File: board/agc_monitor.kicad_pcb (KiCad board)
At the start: 4 copper layers, 149.9 x 74.3 mm, 60 parts, among them J1 Conn_01x03, J2 Conn_01x03, J3 Conn_01x10, J4 Styx_P4, J5 Styx_P5, P1 test_connector, Q1 MMBT3904, Q2 MMBT3904, Q3 MMBT3904, Q4 MMBT3904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

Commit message: Board: Added initial rouuting of 3.3V I/O power
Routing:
- net +3V3_IO: track 25.2 -> 188.0 mm, vias 0 -> 8
- added copper zone on In2.Cu, net +3V3_IO
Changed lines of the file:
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@@
     (thickness 1.6)
     (drawings 9)
-    (tracks 1874)
+    (tracks 1921)
     (zones 0)
     (modules 60)
@@
   )
   (setup
-    (last_trace_width 0.1524)
+    (last_trace_width 0.254)
     (user_trace_width 0.1524)
     (user_trace_width 0.2032)
@@
   (segment (start 190.1825 117.7925) (end 180.4035 117.7925) (width 0.1524) (layer In2.Cu) (net 175))
   (segment (start 180.4035 117.7925) (end 174.5615 123.6345) (width 0.1524) (layer In2.Cu) (net 175))
+  (segment (start 145.415 92.45) (end 144.145 92.45) (width 0.254) (layer B.Cu) (net 175))
+  (segment (start 144.145 92.45) (end 142.875 92.45) (width 0.254) (layer B.Cu) (net 175))
+  (segment (start 142.875 92.45) (end 141.605 92.45) (width 0.254) (layer B.Cu) (net 175))
+  (segment (start 141.605 92.45) (end 136.525 92.45) (width 0.254) (layer B.Cu) (net 175))
+  (segment (start 136.525 92.45) (end 137.795 92.45) (width 0.254) (layer F.Cu) (net 175))
+  (segment (start 137.795 92.45) (end 139.065 92.45) (width 0.254) (layer F.Cu) (net 175))
+  (segment (start 139.065 92.45) (end 145.415 92.45) (width 0.254) (layer F.Cu) (net 175))
+  (segment (start 135.642 92.45) (end 136.525 92.45) (width 0.254) (layer B.Cu) (net 175))
+  (segment (start 135.636 92.456) (end 135.642 92.45) (width 0.254) (layer B.Cu) (net 175))
+  (segment (start 136.519 92.456) (end 136.525 92.45) (width 0.254) (layer F.Cu) (net 175))
+  (via (at 135.636 92.456) (size 0.6096) (drill 0.3048) (layers F.Cu B.Cu) (net 175))
+  (segment (start 135.636 92.456) (end 136.519 92.456) (width 0.254) (layer F.Cu) (net 175))
+  (segment (start 132.461 92.45) (end 123.571 92.45) (width 0.254) (layer F.Cu) (net 175))
+  (segment (start 132.461 92.45) (end 123.571 92.45) (width 0.254) (layer B.Cu) (net 175))
+  (via (at 132.461 91.059) (size 0.6096) (drill 0.3048) (layers F.Cu B.Cu) (net 175))
+  (segment (start 132.461 92.45) (end 132.461 91.059) (width 0.254) (layer B.Cu) (net 175))
+  (segment (start 132.461 91.059) (end 132.461 92.45) (width 0.254) (layer F.Cu) (net 175))
+  (segment (start 119.507 92.45) (end 110.617 92.45) (width 0.254) (layer F.Cu) (net 175))
+  (segment (start 110.617 92.45) (end 119.507 92.45) (width 0.254) (layer B.Cu) (net 175))
+  (via (at 119.507 91.059) (size 0.6096) (drill 0.3048) (layers F.Cu B.Cu) (net 175))
+  (segment (start 119.507 92.45) (end 119.507 91.059) (width 0.254) (layer F.Cu) (net 175))
+  (segment (start 119.507 91.059) (end 119.507 92.45) (width 0.254) (layer B.Cu) (net 175))
+  (segment (start 106.553 92.45) (end 97.663 92.45) (width 0.254) (layer B.Cu) (net 175))
+  (segment (start 97.663 92.45) (end 106.553 92.45) (width 0.254) (layer F.Cu) (net 175))
+  (via (at 106.553 91.059) (size 0.6096) (drill 0.3048) (layers F.Cu B.Cu) (net 175))
+  (segment (start 106.553 92.45) (end 106.553 91.059) (width 0.254) (layer F.Cu) (net 175))
+  (segment (start 106.553 91.059) (end 106.553 92.45) (width 0.254) (layer B.Cu) (net 175))
+  (segment (start 145.415 110.75) (end 136.525 110.75) (width 0.254) (layer F.Cu) (net 175))
+  (segment (start 136.525 110.75) (end 145.415 110.75) (width 0.254) (layer B.Cu) (net 175))
+  (segment (start 132.461 110.75) (end 123.571 110.75) (width 0.254) (layer F.Cu) (net 175))
+  (segment (start 123.571 110.75) (end 132.461 110.75) (width 0.254) (layer B.Cu) (net 175))
+  (segment (start 119.507 110.75) (end 110.617 110.75) (width 0.254) (layer F.Cu) (net 175))
+  (segment (start 110.617 110.75) (end 119.507 110.75) (width 0.254) (layer B.Cu) (net 175))
+  (segment (start 106.553 110.75) (end 97.663 110.75) (width 0.254) (layer B.Cu) (net 175))
+  (segment (start 97.663 110.75) (end 106.553 110.75) (width 0.254) (layer F.Cu) (net 175))
+  (via (at 140.335 112.141) (size 0.6096) (drill 0.3048) (layers F.Cu B.Cu) (net 175))
+  (segment (start 140.335 110.75) (end 140.335 112.141) (width 0.254) (layer F.Cu) (net 175))
+  (segment (start 140.335 112.141) (end 140.335 110.75) (width 0.254) (layer B.Cu) (net 175))
+  (via (at 132.461 112.014) (size 0.6096) (drill 0.3048) (layers F.Cu B.Cu) (net 175))
+  (segment (start 132.461 110.75) (end 132.461 112.014) (width 0.254) (layer B.Cu) (net 175))
+  (segment (start 132.461 112.014) (end 132.461 110.75) (width 0.254) (layer F.Cu) (net 175))
+  (via (at 119.507 112.0775) (size 0.6096) (drill 0.3048) (layers F.Cu B.Cu) (net 175))
+  (segment (start 119.507 110.75) (end 119.507 112.0775) (width 0.254) (layer F.Cu) (net 175))
+  (segment (start 119.507 112.0775) (end 119.507 110.75) (width 0.254) (layer B.Cu) (net 175))
+  (via (at 106.553 111.9505) (size 0.6096) (drill 0.3048) (layers F.Cu B.Cu) (net 175))
+  (segment (start 106.553 110.75) (end 106.553 111.9505) (width 0.254) (layer B.Cu) (net 175))
+  (segment (start 106.553 111.9505) (end 106.553 110.75) (width 0.254) (layer F.Cu) (net 175))
   (segment (start 144.841 72.644) (end 150.622 72.644) (width 0.1524) (layer F.Cu) (net 176))
   (segment (start 143.51 73.975) (end 144.841 72.644) (width 0.1524) (layer F.Cu) (net 176))
@@
       )
     )
+  )
+  (zone (net 175) (net_name +3V3_IO) (layer In2.Cu) (hatch edge 0.508)
+    (connect_pads (clearance 0.254))
+    (min_thickness 0.254)
+    (fill yes (arc_segments 16) (thermal_gap 0.508) (thermal_bridge_width 0.508))
+    (polygon
+      (pts
+        (xy 88.7095 83.566) (xy 150.495 83.566) (xy 150.495 72.39) (xy 172.5295 72.39) (xy 178.8795 66.04)
+        (xy 227.965 66.04) (xy 227.965 139.065) (xy 178.435 139.065) (xy 172.466 130.81) (xy 154.4955 130.81)
+        (xy 154.4955 119.634) (xy 88.7095 119.634)
+      )
+    )

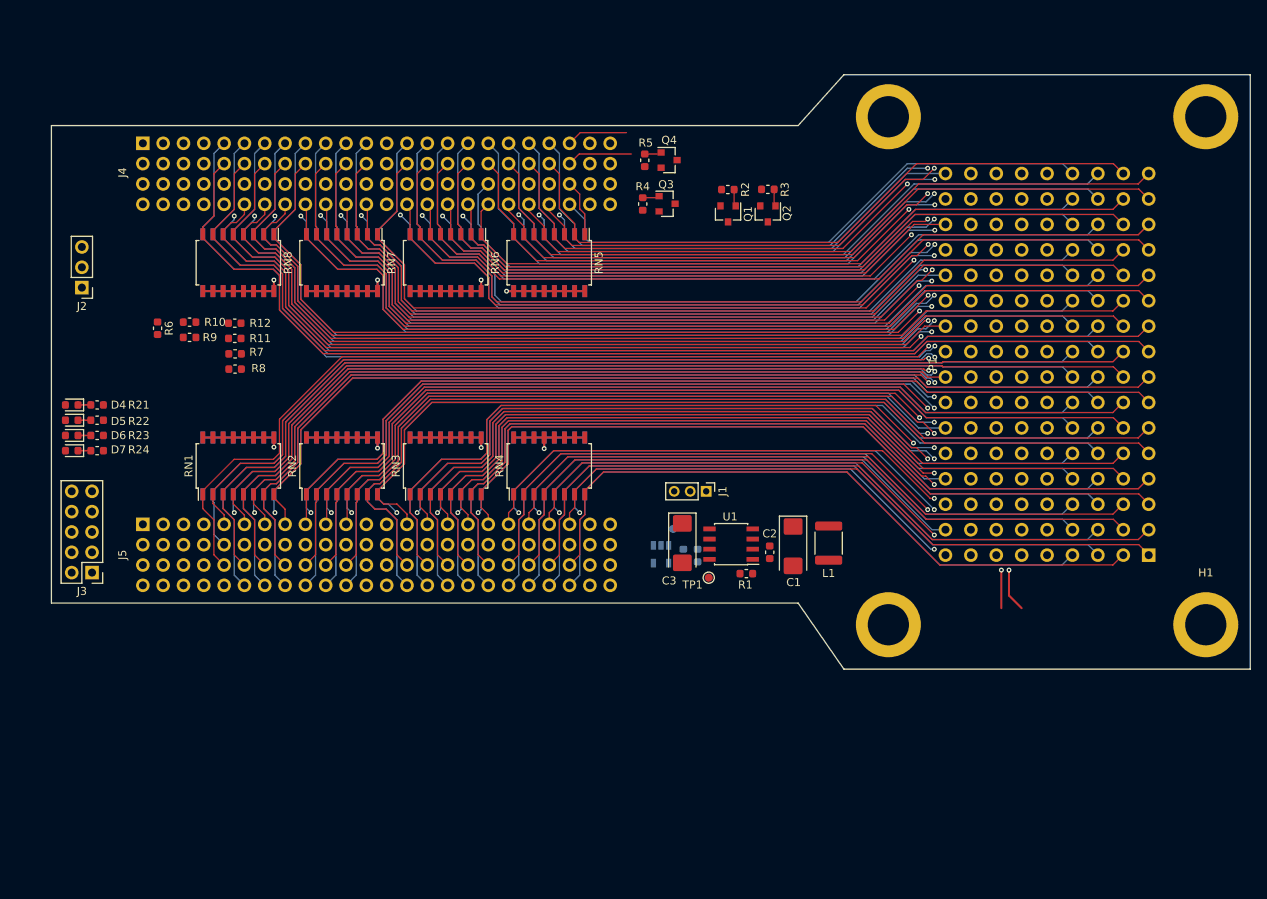
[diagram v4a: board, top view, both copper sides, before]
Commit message: Board: Thinner traces for SI, more layout work, and some 3D models of parts
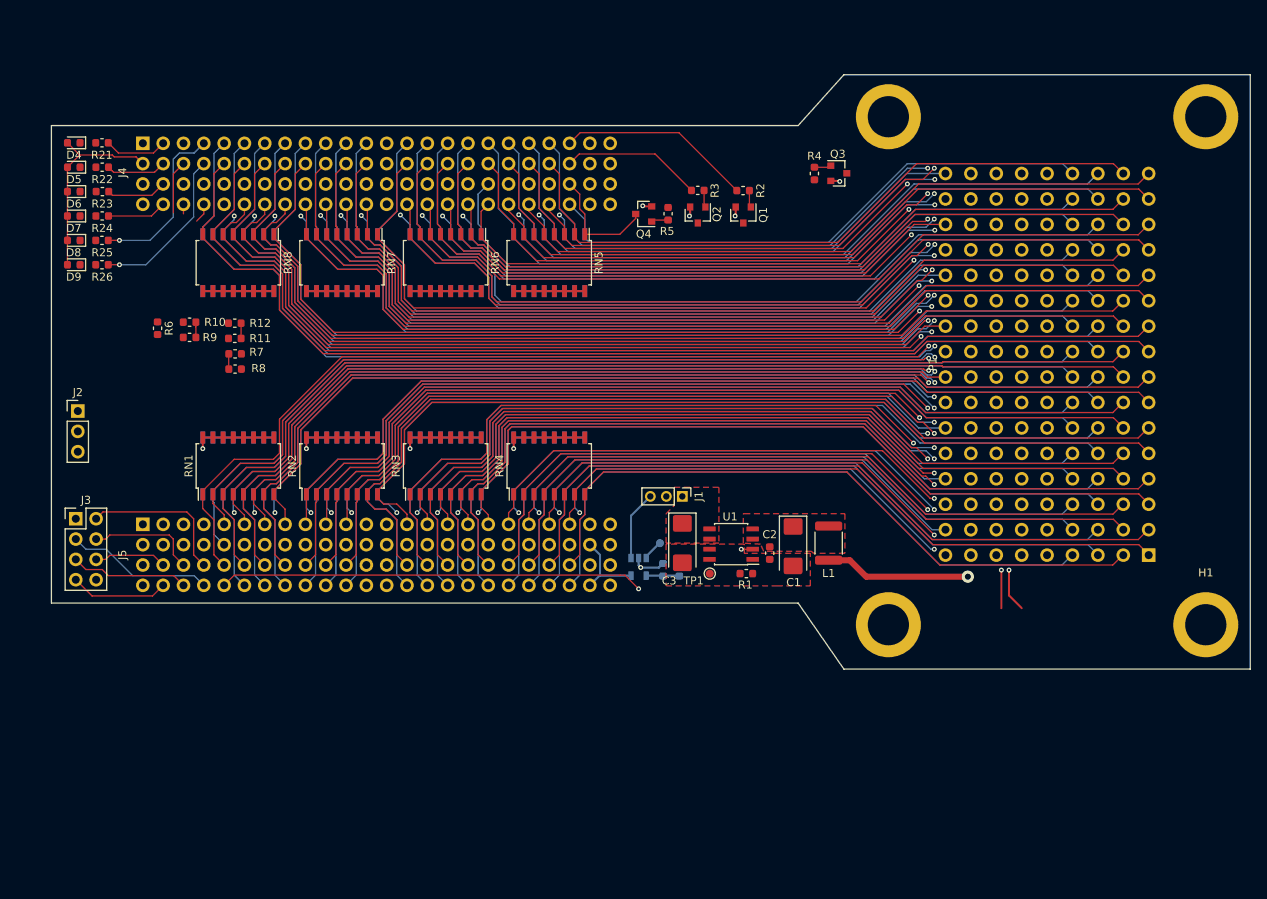
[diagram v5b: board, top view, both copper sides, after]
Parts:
- added D8: LED, LED_SMD:LED_0603_1608Metric, F.Cu at (81.5, 86.1)
- added D9: LED, LED_SMD:LED_0603_1608Metric, F.Cu at (81.5, 89.2)
- added R25: 330, Resistor_SMD:R_0603_1608Metric, F.Cu at (85.1, 86.1)
- added R26: 330, Resistor_SMD:R_0603_1608Metric, F.Cu at (85.1, 89.2)
- J3: value Conn_01x10 -> Conn_01x08; footprint Connector_PinHeader_2.54mm:PinHeader_2x05_P2.54mm_Vertical -> Connector_PinHeader_2.54mm:PinHeader_2x04_P2.54mm_Vertical
- moved R21 32.8 mm to (85.1, 73.9)
- moved D4 32.8 mm to (81.5, 73.9)
- moved R22 31.6 mm to (85.1, 77.0)
- moved D5 31.6 mm to (81.5, 77.0)
- moved R23 30.5 mm to (85.1, 80.0)
- moved D6 30.5 mm to (81.5, 80.0)
- moved R24 29.3 mm to (85.1, 83.1)
- moved D7 29.3 mm to (81.5, 83.1)
- moved Q3 21.8 mm to (177.2, 77.7)
- moved R4 21.8 mm to (174.1, 77.7)
- moved J2 15.4 mm to (82.0, 107.4), turned to 0 degrees
- moved Q2 8.76 mm to (159.5, 82.9)
- moved R3 8.76 mm to (159.5, 79.9)
- moved Q4 7.44 mm to (152.8, 82.8), turned to 180 degrees
- moved R5 7.29 mm to (155.8, 82.8), turned to 90 degrees
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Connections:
- J3 pad 8: /StyxConnectors/DBG7 -> GND
- J4 pad 13: Net-(J4-Pad13) -> /StyxConnectors/LED5
- J4 pad 14: Net-(J4-Pad14) -> /StyxConnectors/LED6
- J4 pad 19: Net-(J4-Pad19) -> GND
- J4 pad 20: Net-(J4-Pad20) -> ADC_3V3_P
- J4 pad 5: Net-(J4-Pad5) -> /StyxConnectors/LED1
- J4 pad 6: Net-(J4-Pad6) -> /StyxConnectors/LED2
- J4 pad 7: Net-(J4-Pad7) -> /StyxConnectors/LED3
- J4 pad 8: Net-(J4-Pad8) -> /StyxConnectors/LED4
- J5 pad 11: Net-(J5-Pad11) -> /StyxConnectors/DBG3
- J5 pad 12: Net-(J5-Pad12) -> /StyxConnectors/DBG4
- J5 pad 15: Net-(J5-Pad15) -> /StyxConnectors/DBG1
- J5 pad 16: Net-(J5-Pad16) -> /StyxConnectors/DBG2
- J5 pad 20: Net-(J5-Pad20) -> EN_3V3_AGC
- J5 pad 7: Net-(J5-Pad7) -> /StyxConnectors/DBG5
- J5 pad 8: Net-(J5-Pad8) -> /StyxConnectors/DBG6
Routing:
- net EN_3V3_AGC: track 0.00 -> 54.5 mm, vias 0 -> 2
- net +3V3_IO: track 188.0 -> 224.9 mm, vias 8 -> 4
- net +3V3_FPGA: track 0.00 -> 34.9 mm
- net +4SW: track 0.00 -> 25.5 mm, vias 0 -> 1
- net /StyxConnectors/LED5: track 0.00 -> 21.2 mm, vias 0 -> 1
- net /StyxConnectors/LED6: track 0.00 -> 20.3 mm, vias 0 -> 1
- net /StyxConnectors/DBG1: track 0.00 -> 19.2 mm
- net /StyxConnectors/DBG2: track 0.00 -> 18.4 mm
- net NHSTRT1: track 7.66 -> 24.5 mm
- net /StyxConnectors/DBG4: track 0.00 -> 14.8 mm
- net /StyxConnectors/DBG3: track 0.00 -> 13.8 mm
- net /StyxConnectors/DBG6: track 0.00 -> 12.3 mm
- net NHSTRT2: track 8.25 -> 17.6 mm
- net /StyxConnectors/DBG5: track 0.00 -> 9.09 mm
- net GND: track 0.00 -> 8.92 mm, vias 0 -> 5
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- added copper zone on F.Cu, net +3V3_AGC
- added copper zone on F.Cu, net GND
- added copper zone on In2.Cu, net GND
- added copper zone on F.Cu, net Net-(C1-Pad1)
- removed copper zone on In2.Cu, net +3V3_FPGA
- removed copper zone on In2.Cu, net +3V3_IO
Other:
- rule trace_min: 0.1524 -> 0.1016

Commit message: Redid the mechanical outline of the board; further development/layout
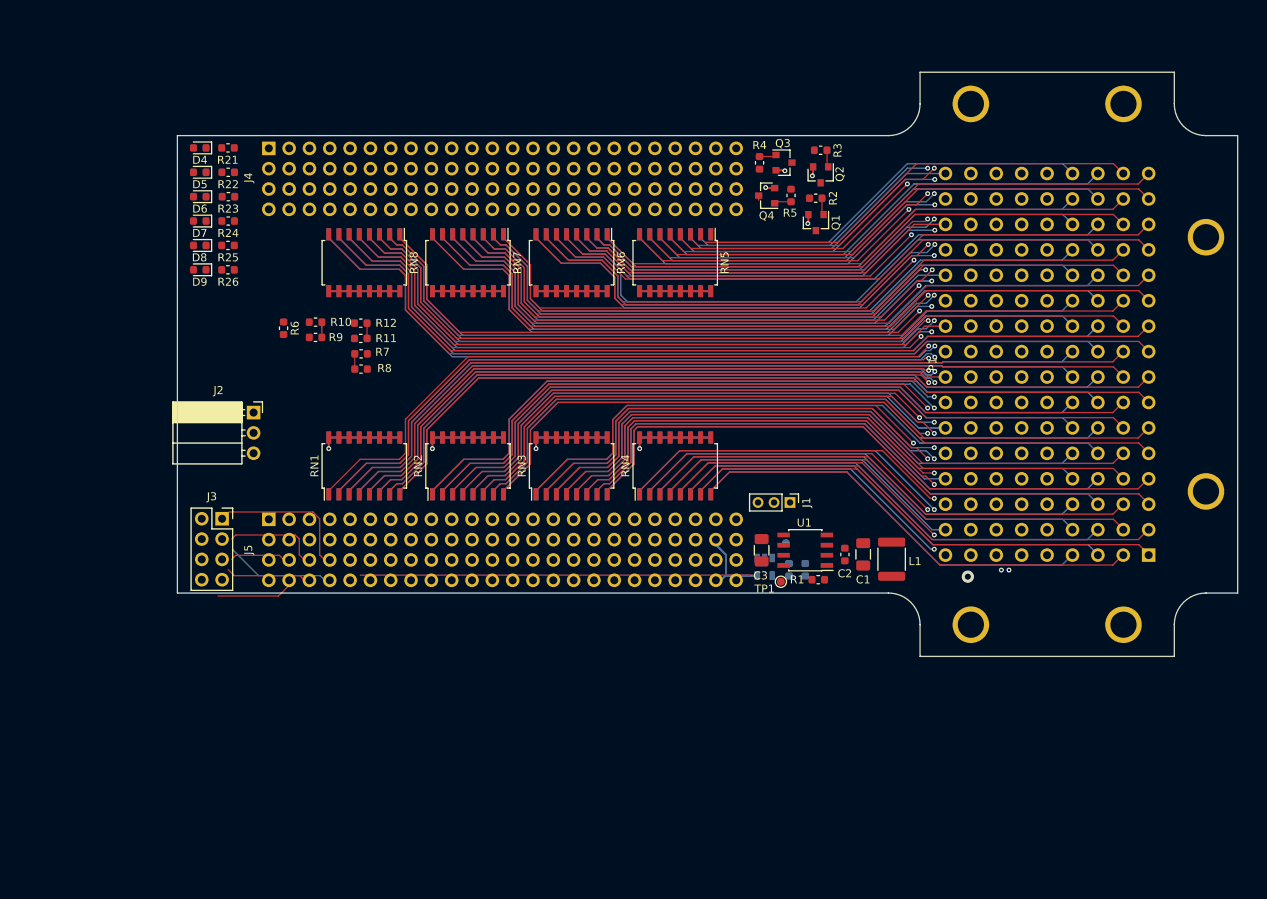
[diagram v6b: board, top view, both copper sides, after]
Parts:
- added H5: MountingHole_Pad, agc_monitor:MountingHole_ANSI_4, F.Cu at (223.1, 85.7)
- added H6: MountingHole_Pad, agc_monitor:MountingHole_ANSI_4, F.Cu at (223.1, 117.5)
- C1, C3: footprint Capacitor_Tantalum_SMD:CP_EIA-6032-28_Kemet-C -> Capacitor_SMD:C_1206_3216Metric
- H1, H2, H3, H4: footprint agc_monitor:MountingHole_1004579 -> agc_monitor:MountingHole_ANSI_4
- J2: footprint Connector_PinHeader_2.54mm:PinHeader_1x03_P2.54mm_Vertical -> Connector_PinSocket_2.54mm:PinSocket_1x03_P2.54mm_Horizontal
- J3: footprint Connector_PinHeader_2.54mm:PinHeader_2x04_P2.54mm_Vertical -> Connector_PinSocket_2.54mm:PinSocket_2x04_P2.54mm_Vertical
- moved H2 71.4 mm to (212.8, 69.0)
- moved H1 71.4 mm to (193.7, 69.0)
- moved H3 64.3 mm to (193.7, 134.2)
- moved H4 64.3 mm to (212.8, 134.2)
- moved J2 22.0 mm to (104.0, 107.6)
- moved J3 18.3 mm to (100.1, 120.9)
- moved Q2 16.2 mm to (174.9, 77.9)
- moved R3 16.2 mm to (174.9, 74.8)
- moved R21 15.8 mm to (100.8, 74.5)
- moved R23 15.8 mm to (100.9, 80.6)
- moved R25 15.8 mm to (100.8, 86.7)
- moved R26 15.8 mm to (100.8, 89.8)
- moved D4 15.8 mm to (97.3, 74.5)
- moved D5 15.8 mm to (97.3, 77.6)
- moved D6 15.8 mm to (97.3, 80.6)
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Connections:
- D4 pad 2: +3V3_FPGA -> /StyxConnectors/3V3_LED
- D5 pad 2: +3V3_FPGA -> /StyxConnectors/3V3_LED
- D6 pad 2: +3V3_FPGA -> /StyxConnectors/3V3_LED
- D7 pad 2: +3V3_FPGA -> /StyxConnectors/3V3_LED
- D8 pad 2: +3V3_FPGA -> /StyxConnectors/3V3_LED
- D9 pad 2: +3V3_FPGA -> /StyxConnectors/3V3_LED
- J4 pad 2: +3V3_FPGA -> /StyxConnectors/3V3_LED
- J4 pad 93: +3V3_FPGA -> Net-(J4-Pad93)
- J4 pad 94: +3V3_FPGA -> Net-(J4-Pad94)
- J4 pad 95: +3V3_FPGA -> Net-(J4-Pad95)
- J4 pad 96: +3V3_FPGA -> Net-(J4-Pad96)
- J5 pad 3: +3V3_FPGA -> Net-(J5-Pad3)
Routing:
- net NHALGA: track 134.1 -> 89.5 mm
- net MRCH: track 103.1 -> 72.6 mm
- net MSQ10: track 125.5 -> 96.3 mm
- net MNISQ: track 118.6 -> 89.4 mm
- net DBLTST: track 110.4 -> 81.2 mm
- net MT09: track 133.7 -> 104.5 mm
- net MSQ13: track 109.7 -> 80.6 mm
- net MPIPAL_n: track 73.6 -> 44.7 mm
- net MOSCAL_n: track 75.5 -> 46.6 mm
- net MVFAIL_n: track 67.8 -> 38.9 mm
- net MWEBG: track 88.7 -> 59.8 mm
- net MWG: track 122.1 -> 93.4 mm
- net MWBG: track 128.8 -> 100.1 mm
- net MT08: track 126.9 -> 98.2 mm
- net MSCDBL_n: track 113.9 -> 85.2 mm
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- removed copper zone on F.Cu, net +3V3_AGC
- removed copper zone on F.Cu, net GND
- removed copper zone on F.Cu, net Net-(C1-Pad1)
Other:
- board size 149.9 x 74.3 mm -> 132.5 x 73 mm

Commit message: Board: completed initial layout
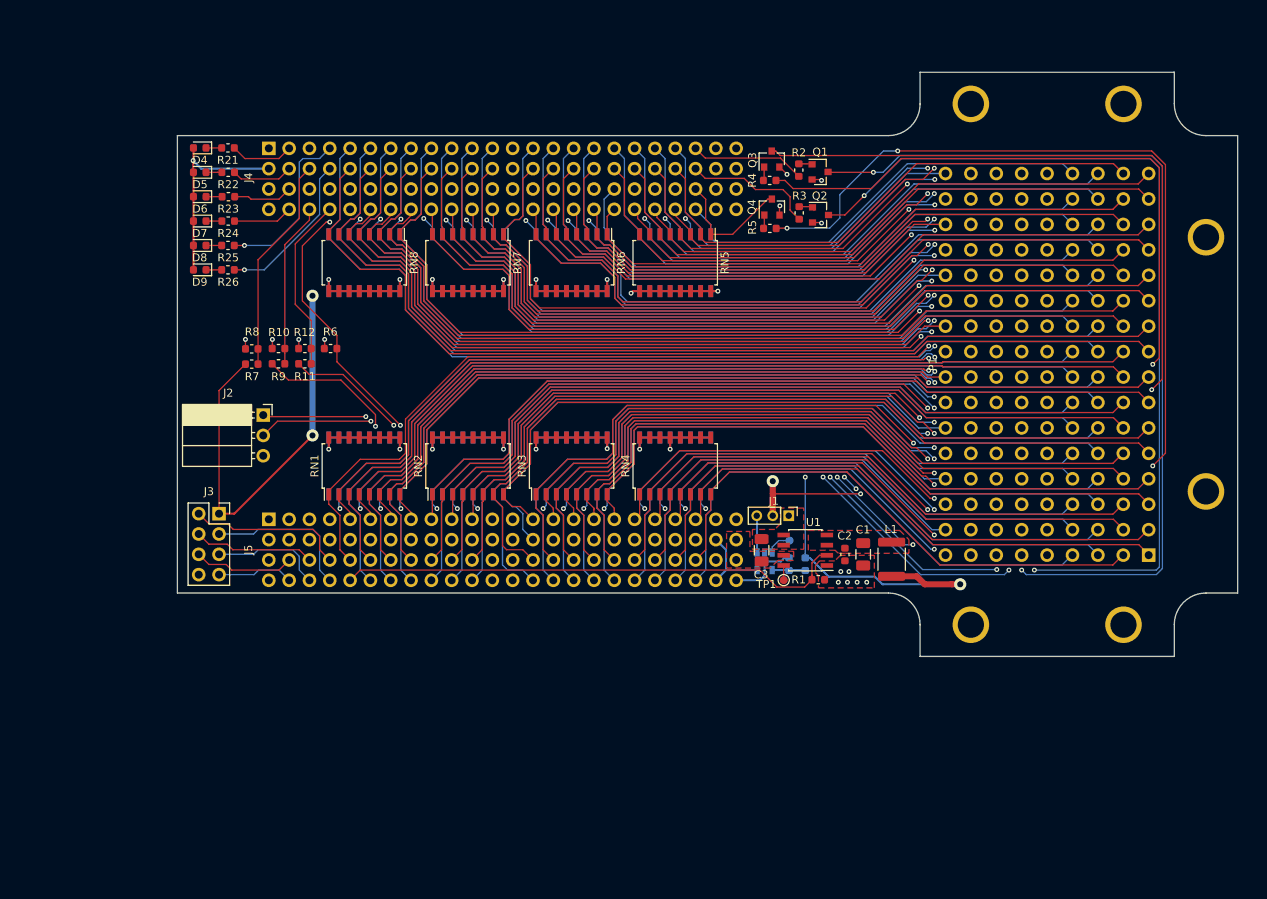
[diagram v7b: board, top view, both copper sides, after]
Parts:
- moved R8 13.9 mm to (103.8, 99.7), turned to 180 degrees
- moved R7 13.7 mm to (103.8, 101.6), turned to 0 degrees
- moved R3 8.28 mm to (172.2, 82.7), turned to 270 degrees
- moved R11 7.67 mm to (110.4, 101.5)
- moved R12 7.67 mm to (110.4, 99.6)
- moved R6 6.41 mm to (113.6, 99.6), turned to 180 degrees
- moved Q1 6.35 mm to (174.8, 77.6), turned to 0 degrees
- moved R10 5.69 mm to (107.1, 99.6)
- moved R9 5.69 mm to (107.1, 101.5)
- moved Q2 5.02 mm to (174.9, 82.9), turned to 0 degrees
- moved R5 4.90 mm to (168.5, 84.6), turned to 0 degrees
- moved R2 4.10 mm to (172.2, 77.3), turned to 270 degrees
- moved R4 2.54 mm to (168.5, 78.6), turned to 0 degrees
- moved J1 1.66 mm to (170.9, 120.5)
- moved Q3 1.59 mm to (168.8, 75.9), turned to 90 degrees
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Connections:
- J4 pad 10: ADC_BPLSSW_P -> ADC_3V3_P
- J4 pad 16: MTLO -> ADC_BPLSSW_P
- J4 pad 20: ADC_3V3_P -> MTLO
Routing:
- net +3V3_IO: track 234.6 -> 397.0 mm, vias 4 -> 20
- net SIGNY: track 0.00 -> 116.8 mm, vias 0 -> 3
- net STRT2: track 0.00 -> 116.1 mm, vias 0 -> 2
- net +4SW: track 7.29 -> 121.9 mm, vias 1 -> 3
- net STRT1: track 0.00 -> 113.5 mm, vias 0 -> 2
- net NHALGA: track 89.5 -> 194.5 mm, vias 1 -> 3
- net CTRL2: track 5.70 -> 107.8 mm, vias 1 -> 3
- net CTRL1: track 2.13 -> 101.8 mm, vias 1 -> 3
- net MTLO: track 17.1 -> 113.7 mm, vias 0 -> 4
- net ALGA: track 0.00 -> 91.8 mm, vias 0 -> 1
- net BPLSSW: track 4.03 -> 93.9 mm, vias 0 -> 3
- net ADC_3V3_P: track 1.91 -> 27.1 mm
- net /StyxConnectors/3V3_LED: track 0.00 -> 25.2 mm, vias 0 -> 1
- net /StyxConnectors/LED5: track 0.00 -> 21.1 mm, vias 0 -> 1
- net ADC_BPLSSW_P: track 1.91 -> 21.9 mm
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- added copper zone on F.Cu, net +3V3_AGC
- added copper zone on F.Cu, net GND
- added copper zone on F.Cu, net Net-(C1-Pad1)
